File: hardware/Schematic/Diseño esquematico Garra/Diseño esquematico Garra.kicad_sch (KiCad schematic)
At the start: 11 parts, among them J1 Screw_Terminal_01x02

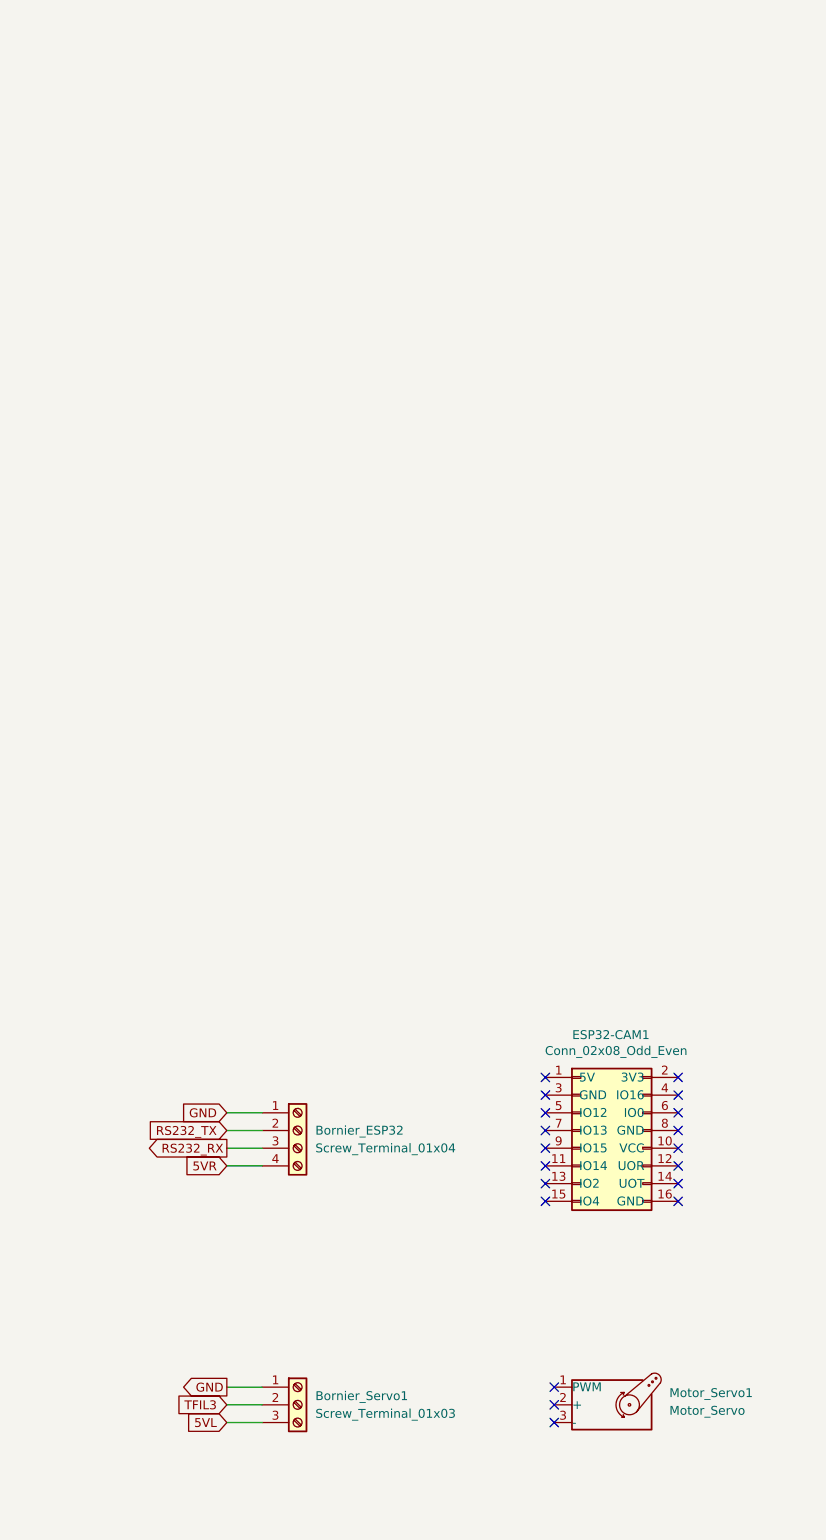
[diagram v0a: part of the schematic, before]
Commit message: ESP32 Schematic implemented
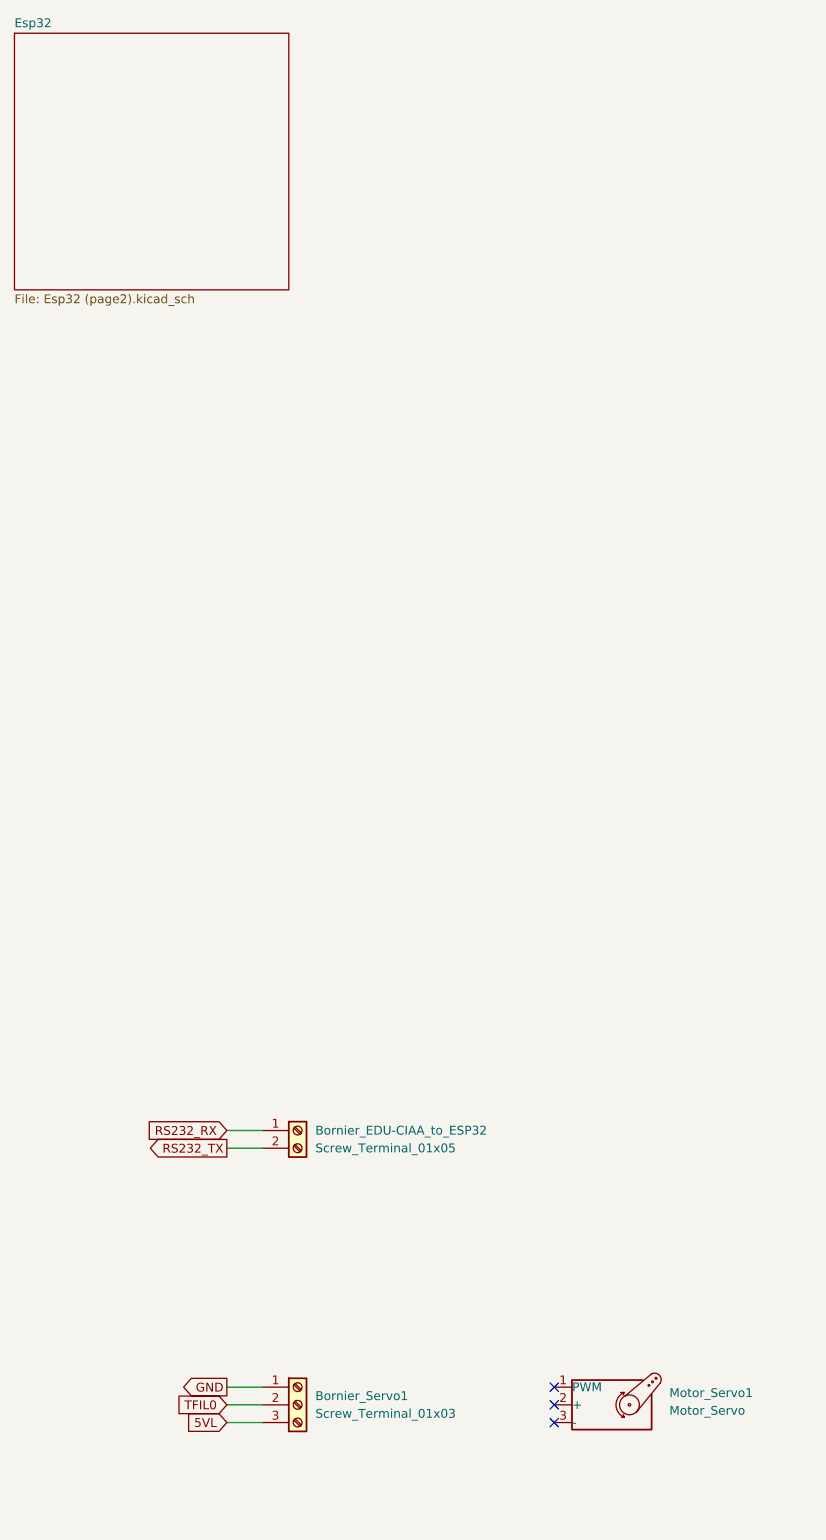
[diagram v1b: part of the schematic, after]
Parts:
- removed Bornier_ESP32: Screw_Terminal_01x04, ProyectoTdL:TerminalBlock_bornier-4_P5.08mm, symbol Connector:Screw_Terminal_01x04
- removed ESP32-CAM1: Conn_02x08_Odd_Even, symbol Connector_Generic:Conn_02x08_Odd_Even
- added Bornier_EDU-CIAA_to_ESP32: Screw_Terminal_01x05, ProyectoTdL:TerminalBlock_bornier-2_P5.08mm, symbol Connector:Screw_Terminal_01x02
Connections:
- net TFIL3 is gone; now on net TFIL0: Bornier_Servo1.2 (Pin_2)
- net RS232_RX: now also Bornier_EDU-CIAA_to_ESP32.1 (Pin_1)
- net RS232_TX: now also Bornier_EDU-CIAA_to_ESP32.2 (Pin_2)
- no-connect marks 19 -> 3
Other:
- added sheet Esp32 (Esp32 (page2).kicad_sch)

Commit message: Fixes to Schematic
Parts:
- added Bornier_Servo2: Screw_Terminal_01x03, ProyectoTdL:TerminalBlock_bornier-3_P5.08mm, symbol Connector:Screw_Terminal_01x03
- added Motor_Servo_Garra: Motor_Servo, symbol Motor:Motor_Servo
- renumbered Motor_Servo1 to Motor_Servo_Z
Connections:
- net 5VL: no longer Bornier_Servo1.3 (Pin_3)
- net GND: now also Bornier_Servo2.1 (Pin_1)
- new net 5V: Bornier_Servo1.3 (Pin_3), Bornier_Servo2.3 (Pin_3)
- new net TFIL3: Bornier_Servo2.2 (Pin_2)
- no-connect marks 3 -> 6
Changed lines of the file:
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@@
+	)
+	(no_connect
+		(at 81.28 97.79)
+	)
+	(no_connect
+		(at 81.28 95.25)
+	)
+	(no_connect
+		(at 81.28 100.33)
 	)
 	(no_connect
@@
 	(wire
 		(pts
+			(xy 34.29 100.33) (xy 39.37 100.33)
+		)
+		(stroke
+			(width 0)
+			(type default)
+		)
+	)
+	(wire
+		(pts
 			(xy 72.39 162.56) (xy 67.31 162.56)
 		)
@@
 	(wire
 		(pts
+			(xy 34.29 97.79) (xy 39.37 97.79)
+		)
+		(stroke
+			(width 0)
+			(type default)
+		)
+	)
+	(wire
+		(pts
 			(xy 140.97 78.74) (xy 140.97 80.01)
 		)
@@
 	(wire
 		(pts
+			(xy 34.29 95.25) (xy 39.37 95.25)
+		)
+		(stroke
+			(width 0)
+			(type default)
+		)
+	)
+	(wire
+		(pts
 			(xy 72.39 124.46) (xy 67.31 124.46)
 		)
@@
 			(width 0)
 			(type default)
-		)
-	)
-	(label "1"
-		(at 260.35 185.42 0)
-		(effects
-			(font
-				(size 1.27 1.27)
-			)
-			(justify left bottom)
 		)
 	)
@@
 		)
 	)
-	(global_label "5VL"
+	(global_label "5V"
 		(shape input)
 		(at 34.29 82.55 180)
@@
 		)
 	)
+	(global_label "TFIL3"
+		(shape input)
+		(at 34.29 97.79 180)
+		(effects
+			(font
+				(size 1.27 1.27)
+			)
+			(justify right)
+		)
+		(property "Intersheetrefs" "${INTERSHEET_REFS}"
+			(at 34.29 97.79 0)
+			(effects
+				(font
+					(size 1.27 1.27)
+				)
+				(hide yes)
+			)
+		)
+	)
 	(global_label "STEP2"
 		(shape output)
@@
 		)
 	)
+	(global_label "5V"
+		(shape input)
+		(at 34.29 100.33 180)
+		(effects
+			(font
+				(size 1.27 1.27)
+			)
+			(justify right)
+		)
+		(property "Intersheetrefs" "${INTERSHEET_REFS}"
+			(at 34.29 100.33 0)
+			(effects
+				(font
+					(size 1.27 1.27)
+				)
+				(hide yes)
+			)
+		)
+	)
 	(global_label "5VL"
 		(shape output)
@@
 		(property "Intersheetrefs" "${INTERSHEET_REFS}"
 			(at 34.29 80.01 0)
+			(effects
+				(font
+					(size 1.27 1.27)
+				)
+				(hide yes)
+			)
+		)
+	)
+	(global_label "GND"
+		(shape output)
+		(at 34.29 95.25 180)
+		(effects
+			(font
+				(size 1.27 1.27)
+			)
+			(justify right)
+		)
+		(property "Intersheetrefs" "${INTERSHEET_REFS}"
+			(at 34.29 95.25 0)
 			(effects
 				(font
@@
 		(dnp no)
 		(fields_autoplaced yes)
-		(property "Reference" "Motor_Servo1"
-			(at 97.79 78.3065 0)
+		(property "Reference" "Motor_Servo_Z"
+			(at 97.79 78.3068 0)
 			(effects
 				(font
@@
 		)
 		(property "Value" "Motor_Servo"
-			(at 97.79 80.8465 0)
+			(at 97.79 80.8468 0)
 			(effects
 				(font
@@
 			(project "Diseño esquematico Garra"
 				(path "/a88248f6-7b70-4a9d-b538-4e8e42a3a066"
-					(reference "Motor_Servo1")
+					(reference "Motor_Servo_Z")
 					(unit 1)
 				)
+			)
+		)
+	)
+	(symbol
+		(lib_id "Motor:Motor_Servo")
+		(at 88.9 97.79 0)
+		(unit 1)
+		(exclude_from_sim no)
+		(in_bom yes)
+		(on_board yes)
+		(dnp no)
+		(fields_autoplaced yes)
+		(property "Reference" "Motor_Servo_Garra"
+			(at 97.79 96.0868 0)
+			(effects
+				(font
+					(size 1.27 1.27)
+				)
+				(justify left)
+			)
+		)
+		(property "Value" "Motor_Servo"
+			(at 97.79 98.6268 0)
+			(effects
+				(font
+					(size 1.27 1.27)
+				)
+				(justify left)
+			)
+		)
+		(property "Footprint" ""
+			(at 88.9 102.616 0)
+			(effects
+				(font
+					(size 1.27 1.27)
+				)
+				(hide yes)
+			)
+		)
+		(property "Datasheet" "http://forums.parallax.com/uploads/attachments/46831/74481.png"
+			(at 88.9 102.616 0)
+			(effects
+				(font
+					(size 1.27 1.27)
+				)
+				(hide yes)
+			)
+		)
+		(property "Description" "Servo Motor (Futaba, HiTec, JR connector)"
+			(at 88.9 97.79 0)
+			(effects
+				(font
+					(size 1.27 1.27)
+				)
+				(hide yes)
+			)
+		)
+		(pin "1"
+		)
+		(pin "3"
+		)
+		(pin "2"
+		)
+		(instances
+			(project "Diseño esquematico Garra"
+				(path "/a88248f6-7b70-4a9d-b538-4e8e42a3a066"
+					(reference "Motor_Servo_Garra")
+					(unit 1)
+				)
+			)
+		)
+	)
+	(symbol
+		(lib_id "Connector:Screw_Terminal_01x03")
+		(at 44.45 97.79 0)
+		(unit 1)
+		(exclude_from_sim no)
+		(in_bom yes)
+		(on_board yes)
+		(dnp no)
+		(fields_autoplaced yes)
+		(property "Reference" "Bornier_Servo2"
+			(at 46.99 96.5199 0)
+			(effects
+				(font
+					(size 1.27 1.27)
+				)
+				(justify left)
+			)
+		)
+		(property "Value" "Screw_Terminal_01x03"
+			(at 46.99 99.0599 0)
+			(effects
+				(font
+					(size 1.27 1.27)
+				)
+				(justify left)
+			)
+		)
+		(property "Footprint" "ProyectoTdL:TerminalBlock_bornier-3_P5.08mm"
+			(at 44.45 97.79 0)
+			(effects
+				(font
+					(size 1.27 1.27)
+				)
+				(hide yes)
+			)
+		)
+		(property "Datasheet" "~"
+			(at 44.45 97.79 0)
+			(effects
+				(font
+					(size 1.27 1.27)
+				)
+				(hide yes)
+			)
+		)
+		(property "Description" "Generic screw terminal, single row, 01x03, script generated (kicad-library-utils/schlib/autogen/connector/)"
+			(at 44.45 97.79 0)
+			(effects
+				(font
+					(size 1.27 1.27)
+				)
+				(hide yes)
+			)
+		)
+		(pin "1"
+		)
+		(pin "3"
+		)
+		(pin "2"
+		)
+		(instances
+			(project "Diseño esquematico Garra"
+				(path "/a88248f6-7b70-4a9d-b538-4e8e42a3a066"
+					(reference "Bornier_Servo2")
+					(unit 1)
+				)

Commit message: Schematics updated + PCB
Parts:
- added Alimentacion_EDU-CIAA: WM4200-ND, ~, symbol edu-ciaa-nxp:CONN_2
- added U2: ESP32-WROOM-32, RF_Module:ESP32-WROOM-32, symbol RF_Module:ESP32-WROOM-32
- CIAA-P1: renamed from CIAA-P1-1; value Conn_02x20_Odd_Even -> ~
- CIAA-P2: renamed from CIAA-P2-1; value Conn_02x20_Odd_Even -> ~
- Motor_DC_Eje_Z: renamed from Motor_Servo_Z; value Motor_Servo -> Motor_N20
- Motor_Servo_Garra: value Motor_Servo -> Motor_Servo_sg90
- renumbered J1 to Poncho_volt_entry_12V
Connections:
- net 3V3L: no longer DRV8825_1.13 (~{RST}), DRV8825_1.14 (~{SLP}), DRV8825_2.13 (~{RST}), DRV8825_2.14 (~{SLP})
- net DIR1: now also CIAA-P2.29 (GPIO0); no longer CIAA-P2.40 (GPIO8)
- net EN1: now also CIAA-P2.33 (GPIO4); no longer CIAA-P2.36 (GPIO5)
- net GND: now also Alimentacion_EDU-CIAA.GND (P1), U2.1 (GND), U2.15 (GND), U2.38 (GND), U2.39 (GND); no longer DRV8825_1.1 (GND), DRV8825_1.7 (GND), Poncho_volt_entry_12V.2 (Pin_2)
- net STEP1: now also CIAA-P2.31 (GPIO2); no longer CIAA-P2.38 (GPIO7)
- net TFIL3: now also CIAA-P1.35 (TFIL3)
- net 5V renamed +5V_ext
- net +5V_ext: now also DRV8825_1.13 (~{RST}), DRV8825_1.14 (~{SLP}), DRV8825_2.13 (~{RST}), DRV8825_2.14 (~{SLP}), U2.2 (VDD); no longer Bornier_Servo1.3 (Pin_3)
- new net 6V: Bornier_Servo1.3 (Pin_3)
- new net GND_A: DRV8825_1.7 (GND), Poncho_volt_entry_12V.2 (Pin_2)
- new net GND_L: DRV8825_1.1 (GND)
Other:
- removed sheet Esp32
- moved on the sheet: Bornier_EDU-CIAA_to_ESP32, Bornier_Nema17_1, Bornier_Nema17_2, Bornier_Servo1, Bornier_Servo2, CIAA-P1, CIAA-P2, DRV8825_1, DRV8825_2, Motor_Servo_Garra, Poncho_volt_entry_12V
